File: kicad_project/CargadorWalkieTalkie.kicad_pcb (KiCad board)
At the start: 2 copper layers, 64 x 31 mm, 9 parts, among them J1 Screw_Terminal_01x02, J2 Screw_Terminal_01x02

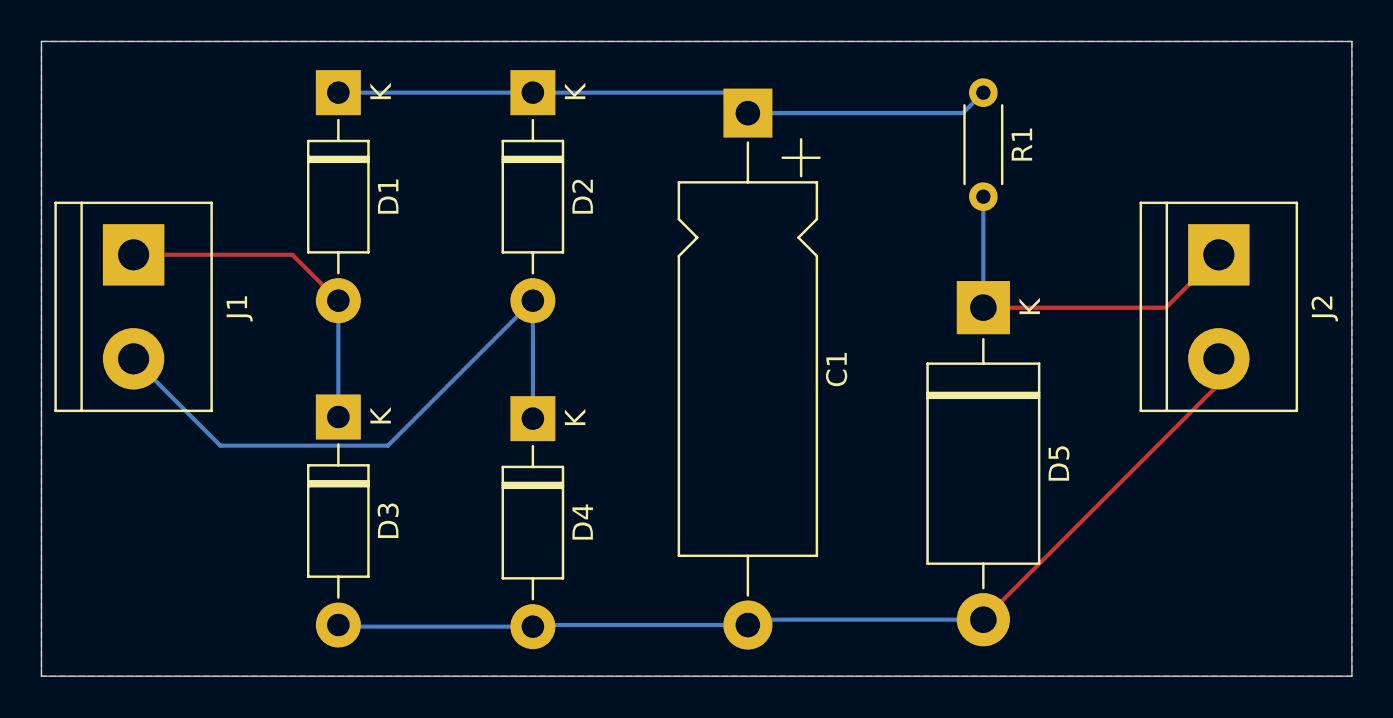
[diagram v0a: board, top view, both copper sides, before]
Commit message: Agregando modelo 3D de los terminales y eliminando rutas redundantes
Signed-off-by: RoMadrigal <rmadrigalmontes@gmail.com>
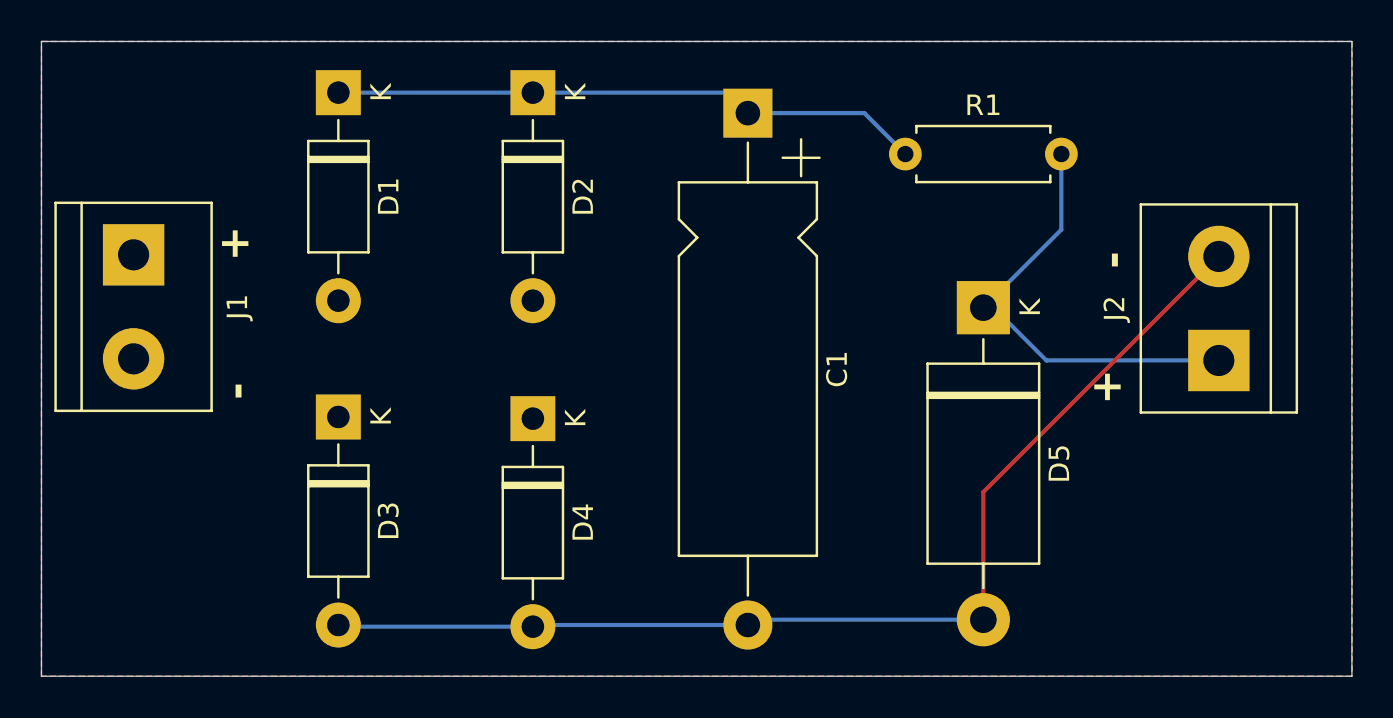
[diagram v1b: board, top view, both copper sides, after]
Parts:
- R1: footprint Resistor_THT:R_Axial_DIN0204_L3.6mm_D1.6mm_P5.08mm_Horizontal -> Resistor_THT:R_Axial_DIN0207_L6.3mm_D2.5mm_P7.62mm_Horizontal
- moved J2 5.16 mm to (148.5, 91.1), turned to 90 degrees
- moved R1 4.85 mm to (133.2, 81.0), turned to 0 degrees
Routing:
- net /gnd: track 29.9 -> 0.00 mm
- net /Vs: track 16.6 -> 0.00 mm
- net Net-(D3-A): track 49.2 -> 54.2 mm
- net Net-(D5-K): track 18.0 -> 21.6 mm
- net Net-(D1-K): track 32.3 -> 28.9 mm
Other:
- board text added: "+"
- board text added: "-"
- board text added: "- anthonycalvo50@gmail.com"
- board text added: "- rmadrigalmontes@gmail.com"
